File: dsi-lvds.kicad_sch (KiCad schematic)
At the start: 55 parts, among them J14 F52R-1A7H1-11020, J15 Conn_FFC_Amphenol_62684-40210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, U16 SN65DSI84

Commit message: [#54231] Add DSI/LVDS converter
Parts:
- removed C62, C63, C66, C67, C68, C69: C_100n_0402, antmicro-footprints:C_0402_1005Metric, symbol antmicroCapacitors0402:C_100n_0402
- removed C65: C_4u7_0402, antmicro-footprints:C_0402_1005Metric, symbol antmicroCapacitors0402:C_4u7_0402
- removed D22, D23, D24, D25, D26, D27, D28: PUSB3F96X_PASS, antmicro-footprints:Nexperia_DFN-10_2.5x1mm_P0.5mm, symbol antmicroTVSDiodes:PUSB3F96X_PASS
- removed J14: F52R-1A7H1-11020, antmicro-footprints:F52R-1A7H1-11020, symbol antmicroFCCConnectors:F52R-1A7H1-11020
- removed J15: Conn_FFC_Amphenol_62684-402100AHLF, antmicro-footprints:Conn_FFC_Amphenol_1x40_62684-402100AHLF, symbol antmicroFCCConnectors:FFC_Amphenol_1x40_62684-402100AHLF
- removed L10, L11, L12, L13, L14, L15, L16, L17, L18, L19, L20, L21, L22, L8, L9: NFP0QHB242HS2D, antmicro-footprints:Choke_025020_0605Metric, symbol antmicroCommonModeChokes:Choke_NFP0QHB242HS2D
- removed R106, R107, R109, R118, R120: R_10k_0402, antmicro-footprints:R_0402_1005Metric, symbol antmicroResistors0402:R_10k_0402
- removed R108, R117, R119, R121: R_0R_0402, antmicro-footprints:R_0402_1005Metric, symbol antmicroResistors0402:R_0R_0402
- removed R112, R113, R114, R115: R_2k2_0402, antmicro-footprints:R_0402_1005Metric, symbol antmicroResistors0402:R_2k2_0402
- removed TP12, TP13: TP_1.5mm_SMD, antmicro-footprints:TP_SMD_1.5mm, symbol antmicroTestPoints:TP_1.5mm_SMD
- removed TP14, TP15, TP16, TP17, TP18, TP19, TP20, TP21: TP_0.75mm_SMD, antmicro-footprints:TP_SMD_0.75mm, symbol antmicroTestPoints:TP_0.75mm_SMD
- added C? (x2): C_1u_0402, antmicro-footprints:C_0402_1005Metric, symbol antmicroCapacitors0402:C_1u_0402
- added C? (x5): C_100n_0402, antmicro-footprints:C_0402_1005Metric, symbol antmicroCapacitors0402:C_100n_0402
- added C? (x3): C_10n_0402, antmicro-footprints:C_0402_1005Metric, symbol antmicroCapacitors0402:C_10n_0402
- added C?: C_10u_0402, antmicro-footprints:C_0402_1005Metric, symbol antmicroCapacitors0402:C_10u_0402
- added FB?: 220Z/2A, antmicro-footprints:FB_0603_1608Metric, symbol antmicroFerriteBeadsandChips:FB_220Z_2.2A_TDK-MPZ_0603
- added R? (x3): R_10k_0402, antmicro-footprints:R_0402_1005Metric, symbol antmicroResistors0402:R_10k_0402
- added R? (x2): R_4k7_0402, antmicro-footprints:R_0402_1005Metric, symbol antmicroResistors0402:R_4k7_0402
- added U?: TXB0104_UQFN, antmicro-footprints:UQFN-12_2x1.7mm_P0.4mm_Texas_RUT, symbol antmicroLogicTranslatorsLevelShifters:TXB0104_UQFN
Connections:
- net SoMtoDisplay_Ferr_D3_N is gone; now on net DSI.D3_N: U16.30 (DA3N)
- net +3V3: now also C?.2, U?.11 (VCCB)
- net DSI.CLK_N: now also U16.25 (DACN)
- net DSI.CLK_P: now also U16.24 (DACP)
- net DSI.D0_N: now also U16.20 (DA0N)
- net DSI.D0_P: now also U16.19 (DA0P)
- net DSI.D1_N: now also U16.22 (DA1N)
- net DSI.D1_P: now also U16.21 (DA1P)
- net DSI.D2_N: now also U16.28 (DA2N)
- net DSI.D2_P: now also U16.27 (DA2P)
- net DSI.D3_P: now also U16.29 (DA3P)
- net GND: now also U16.23 (GND), U16.26 (GND), U16.52 (GND), U16.65 (PAD), C?.1, C?.1, C?.1, C?.1, C?.1, C?.1, C?.1, C?.1, C?.1, C?.1, C?.1, R?.1, R?.2, U?.6 (GND)
- net LVDS.CLK_N: now reaches U16.39 (A_CLKN)
- net at U16.14 (VCC), U16.18 (VCC), U16.3 (VCC)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: now also C?.2, C?.2, C?.2, C?.2, C?.2, C?.2, C?.2, C?.2, FB?.2
- net at U16.17 (REFCLK): now also R?.1
- net DSI/LVDS.EN: now reaches U16.2 (EN)
- net DSI/LVDS.EN: now also U?.4 (A3), U?.8 (B3)
- net at U16.31 (VCORE): now also C?.2
- net DSI/LVDS.IRQ: now reaches U16.33 (IRQ)
- net DSI/LVDS.IRQ: now also U?.5 (A4), U?.7 (B4)
- net LVDS.D3_P: now reaches U16.36 (A_Y3P)
- net LVDS.D3_N: now reaches U16.37 (A_Y3N)
- net LVDS.CLK_P: now reaches U16.38 (A_CLKP)
- net LVDS.D2_P: now reaches U16.41 (A_Y2P)
- net LVDS.D2_N: now reaches U16.42 (A_Y2N)
- net LVDS.D1_P: now reaches U16.44 (A_Y1P)
- net LVDS.D1_N: now reaches U16.45 (A_Y1N)
- net LVDS.D0_P: now reaches U16.46 (A_Y0P)
- net LVDS.D0_N: now reaches U16.47 (A_Y0N)
- net at U16.64 (ADDR): now also R?.1, R?.2
- net I_{2}C_DSI/LVDS.SCL renamed DSI/LVDS.SCL
- net DSI/LVDS.SCL: now also R?.1, U?.3 (A2), U?.9 (B2)
- net I_{2}C_DSI/LVDS.SDA renamed DSI/LVDS.SDA
- net DSI/LVDS.SDA: now also R?.1, U?.10 (B1), U?.2 (A1)
- new net +1V8: C?.2, FB?.1, R?.2, R?.2, R?.2, U?.1 (VCCA), U?.12 (OE)
- no-connect marks 3 -> 10
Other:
- note added: "Note: I_{2}C address selection: ADDR | write address 1 | 0x5A 0 | 0x58"
- note added: "Note: SN65DSI83*-Q1 should be here drop-in compatible"
- note removed: "Global reset (active low)"
- note removed: "LVDS connector"
- note removed: "Max 45mA"
- note removed: "Set display orientation as NORMAL datasheet pg.10"
- note removed: "TODO"
- note removed: "VDD"
- note removed: "Vcom"
- note removed: "assembly option for DSI connector (eg. pass-through to LVDS converter)"
- note removed: "select 8bit input"
- note removed: "select normal operation"

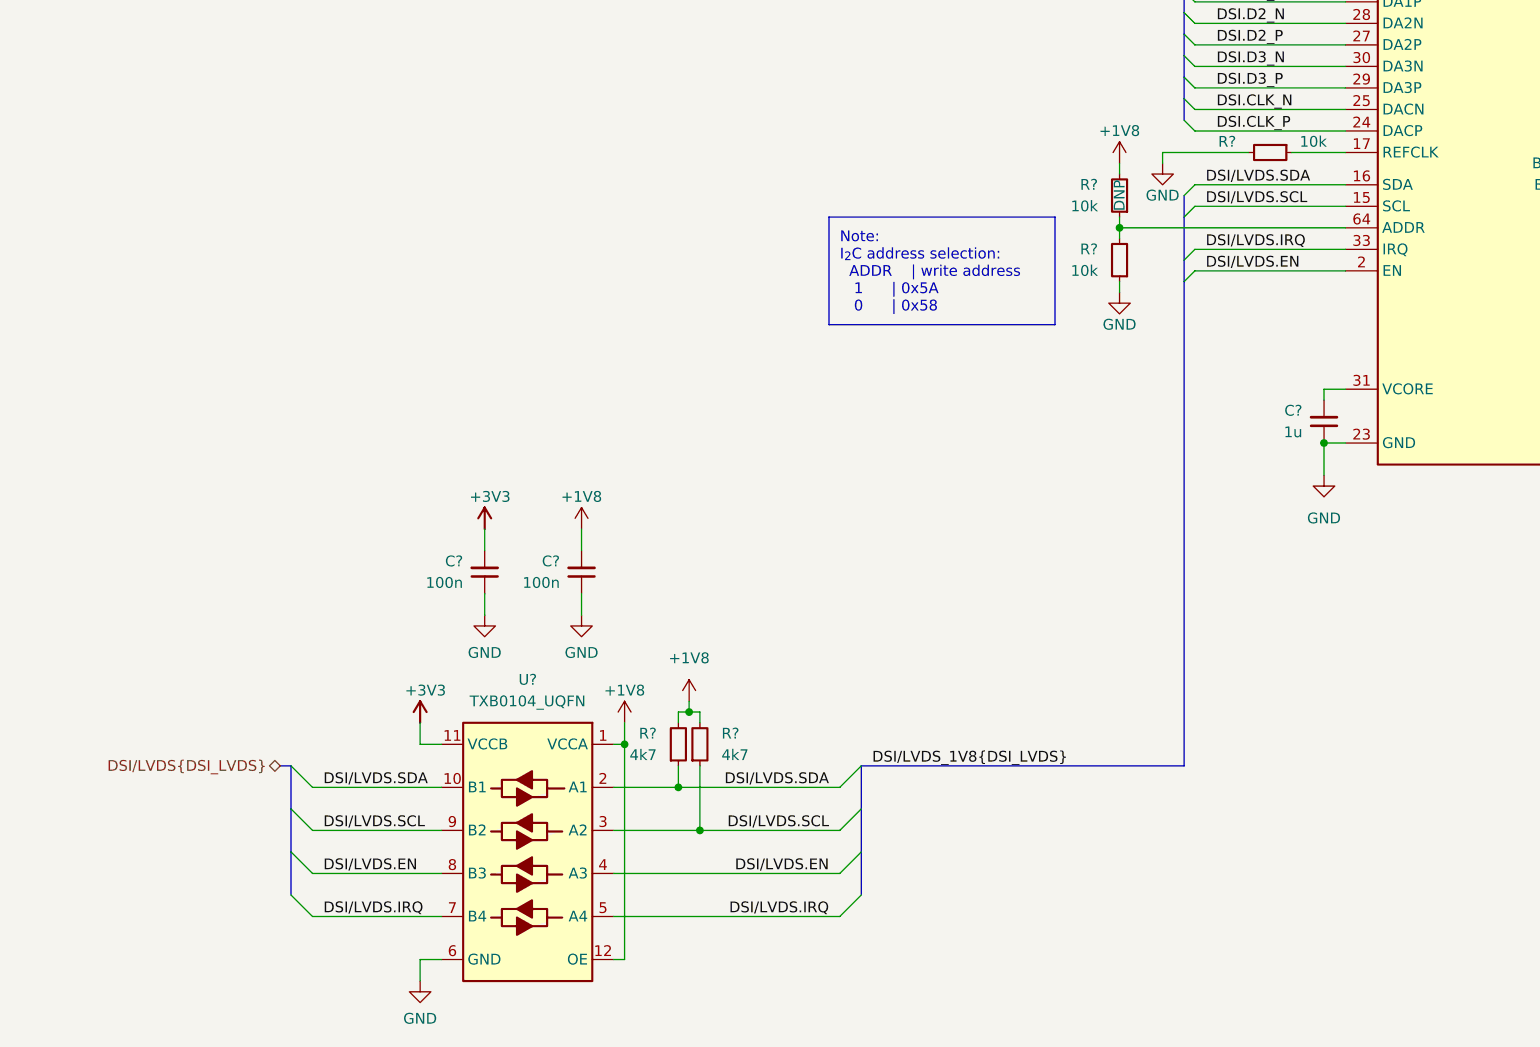
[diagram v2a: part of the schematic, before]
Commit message: [#54231] Rename bus DSI/LVDS to DisplayCtrl
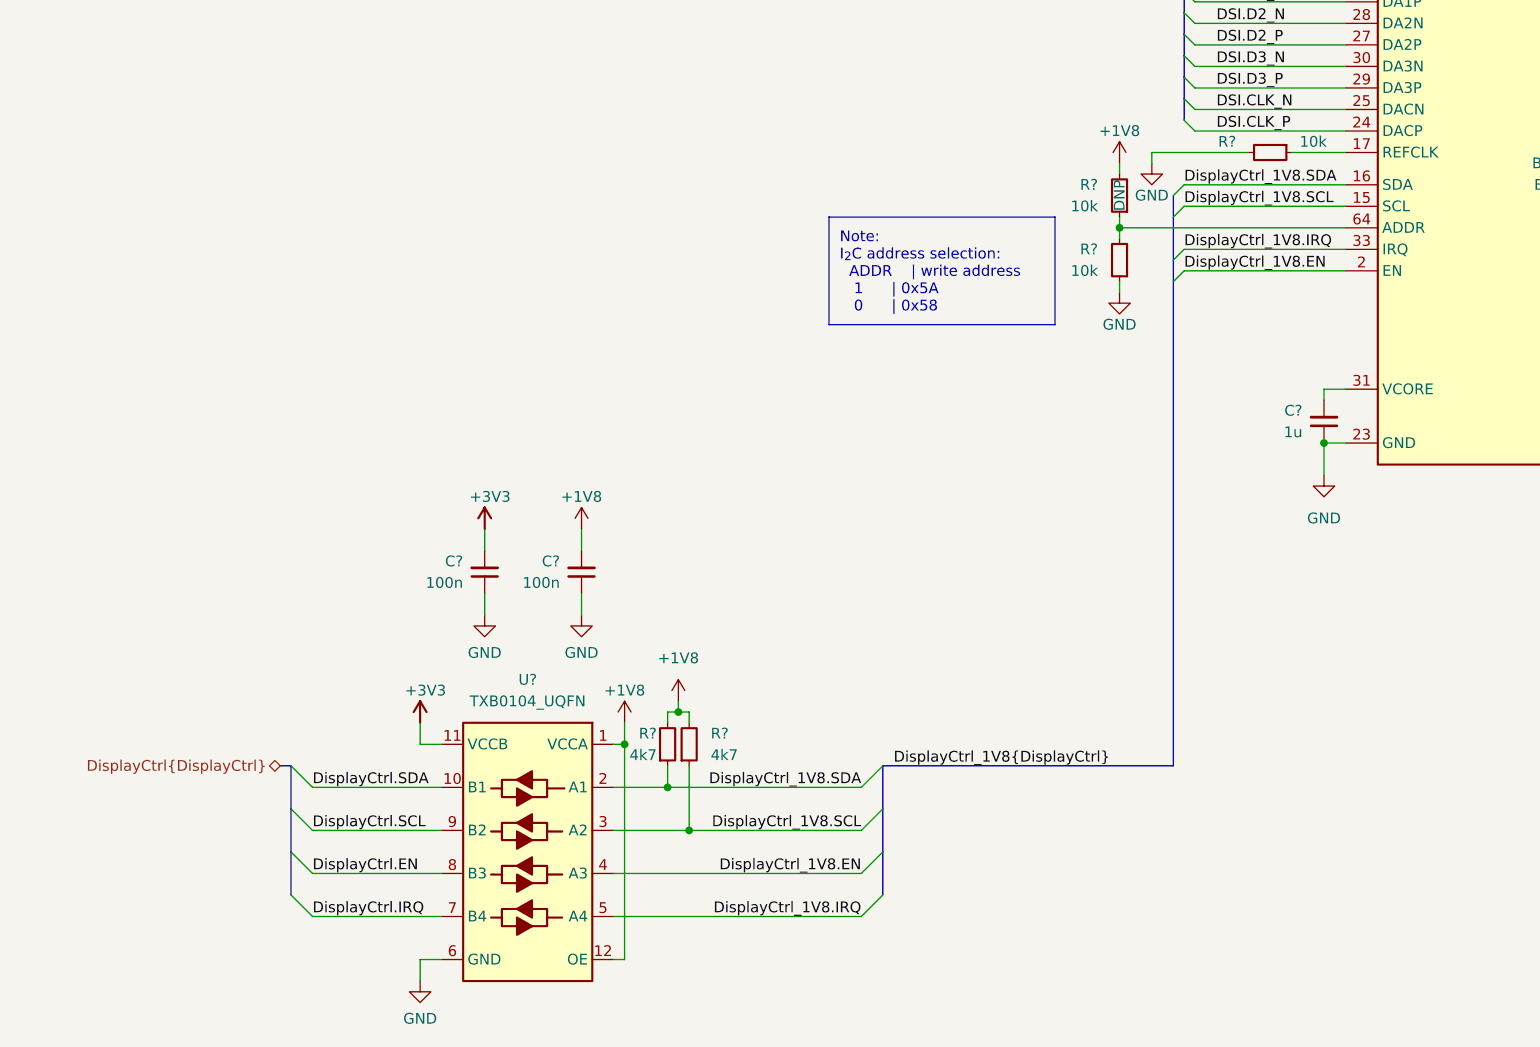
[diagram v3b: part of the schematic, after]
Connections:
- net DSI/LVDS.EN renamed DisplayCtrl_1V8.EN
- net DisplayCtrl_1V8.EN: no longer U?.8 (B3)
- net DSI/LVDS.IRQ renamed DisplayCtrl_1V8.IRQ
- net DisplayCtrl_1V8.IRQ: no longer U?.7 (B4)
- net DSI/LVDS.SCL renamed DisplayCtrl_1V8.SCL
- net DisplayCtrl_1V8.SCL: no longer U?.9 (B2)
- net DSI/LVDS.SDA renamed DisplayCtrl_1V8.SDA
- net DisplayCtrl_1V8.SDA: no longer U?.10 (B1)
- new net DisplayCtrl.EN: U?.8 (B3)
- new net DisplayCtrl.IRQ: U?.7 (B4)
- new net DisplayCtrl.SCL: U?.9 (B2)
- new net DisplayCtrl.SDA: U?.10 (B1)
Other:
- moved on the sheet: R?

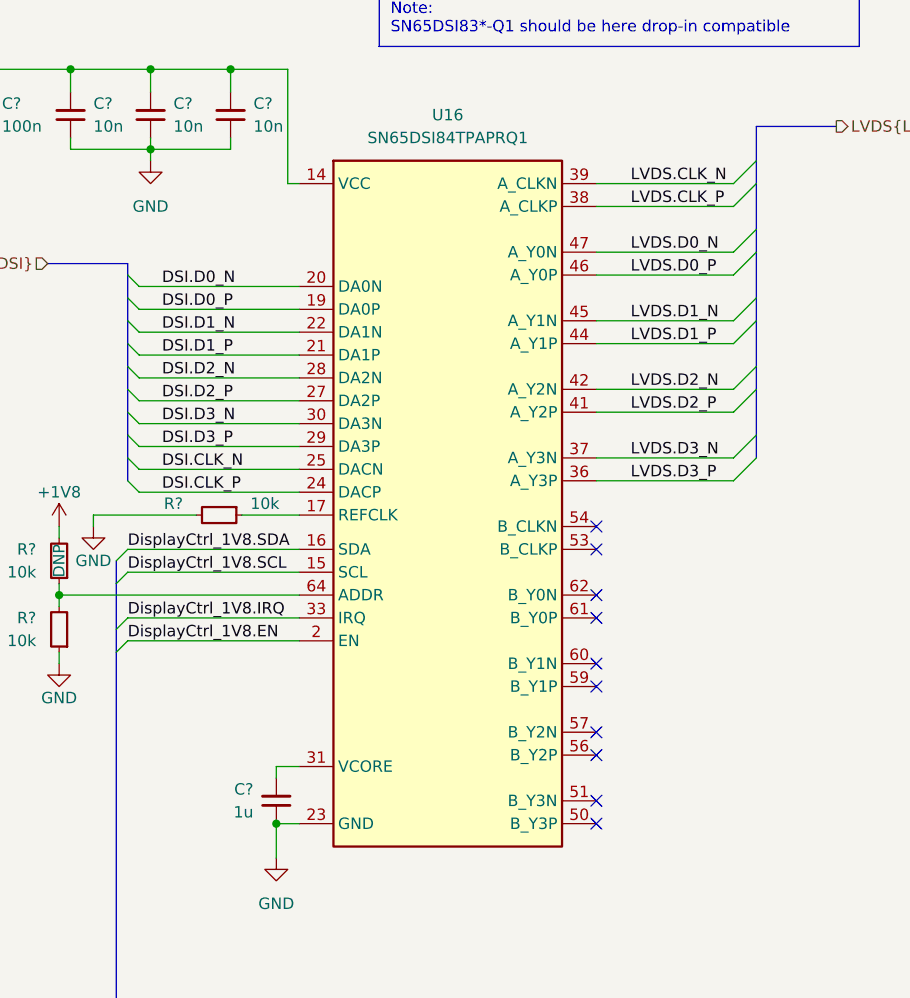
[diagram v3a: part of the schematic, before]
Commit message: [#54617] Update SN65DSI84 symbol
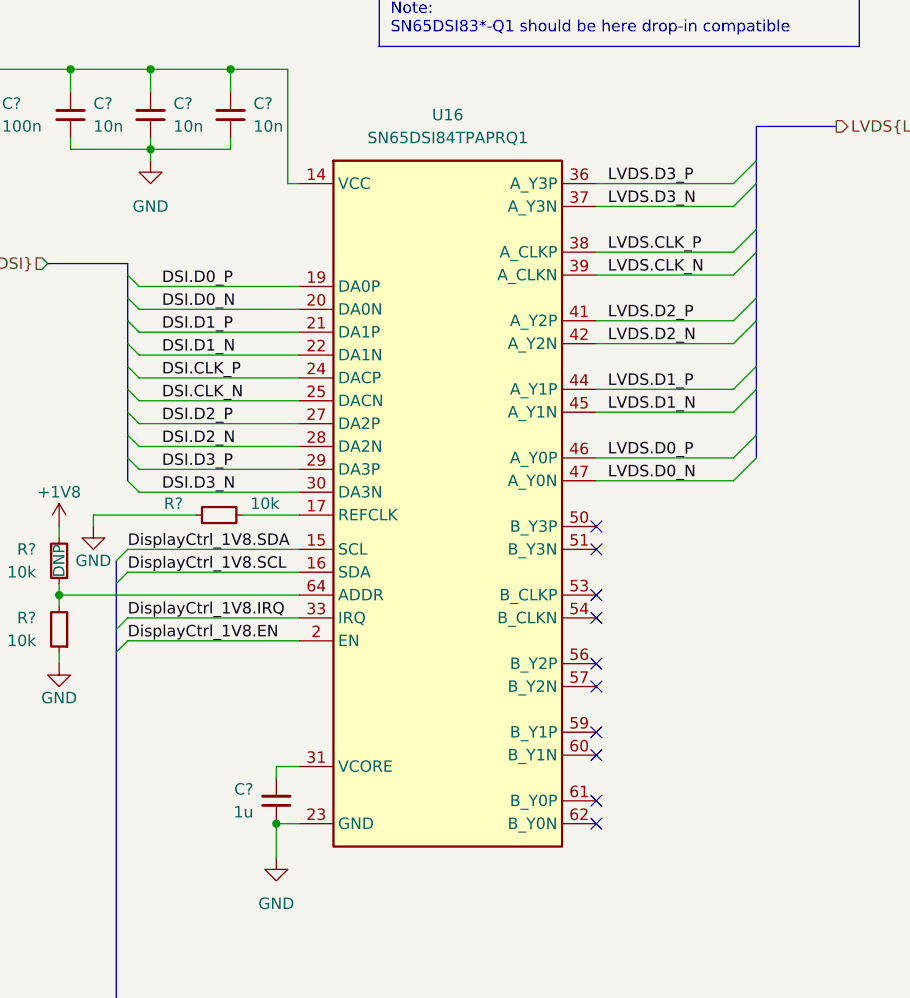
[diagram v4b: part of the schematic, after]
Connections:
- net DisplayCtrl_1V8.SCL: now also U16.16 (SDA); no longer U16.15 (SCL)
- net DisplayCtrl_1V8.SDA: now also U16.15 (SCL); no longer U16.16 (SDA)
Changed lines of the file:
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@@
     (effects (font (size 1.27 1.27)) (justify left bottom))
   )
-  (label "DSI.D3_P" (at 231.14 120.65 0)
+  (label "DSI.D3_P" (at 231.14 123.19 0)
     (effects (font (size 1.27 1.27)) (justify left bottom))
   )
-  (label "LVDS.D0_N" (at 283.21 99.06 0)
+  (label "LVDS.D0_N" (at 280.67 124.46 0)
     (effects (font (size 1.27 1.27)) (justify left bottom))
   )
-  (label "LVDS.D2_N" (at 283.21 114.3 0)
+  (label "LVDS.D2_N" (at 280.67 109.22 0)
     (effects (font (size 1.27 1.27)) (justify left bottom))
   )
@@
     (effects (font (size 1.27 1.27)) (justify left bottom))
   )
-  (label "LVDS.D1_N" (at 283.21 106.68 0)
+  (label "LVDS.D1_N" (at 280.67 116.84 0)
     (effects (font (size 1.27 1.27)) (justify left bottom))
   )
@@
     (effects (font (size 1.27 1.27)) (justify right bottom))
   )
-  (label "LVDS.CLK_P" (at 283.21 93.98 0)
+  (label "LVDS.CLK_P" (at 280.67 99.06 0)
     (effects (font (size 1.27 1.27)) (justify left bottom))
   )
-  (label "DSI.D1_P" (at 231.14 110.49 0)
+  (label "DSI.D1_P" (at 231.14 107.95 0)
     (effects (font (size 1.27 1.27)) (justify left bottom))
   )
-  (label "LVDS.D1_P" (at 283.21 109.22 0)
+  (label "LVDS.D1_P" (at 280.67 114.3 0)
     (effects (font (size 1.27 1.27)) (justify left bottom))
   )
-  (label "LVDS.D3_N" (at 283.21 121.92 0)
+  (label "LVDS.D3_N" (at 280.67 93.98 0)
     (effects (font (size 1.27 1.27)) (justify left bottom))
   )
-  (label "LVDS.CLK_N" (at 283.21 91.44 0)
+  (label "LVDS.CLK_N" (at 280.67 101.6 0)
     (effects (font (size 1.27 1.27)) (justify left bottom))
   )
-  (label "DSI.CLK_P" (at 231.14 125.73 0)
+  (label "DSI.CLK_P" (at 231.14 113.03 0)
     (effects (font (size 1.27 1.27)) (justify left bottom))
   )
@@
     (effects (font (size 1.27 1.27)) (justify left bottom))
   )
-  (label "LVDS.D0_P" (at 283.21 101.6 0)
+  (label "LVDS.D0_P" (at 280.67 121.92 0)
     (effects (font (size 1.27 1.27)) (justify left bottom))
   )
-  (label "LVDS.D2_P" (at 283.21 116.84 0)
+  (label "LVDS.D2_P" (at 280.67 106.68 0)
     (effects (font (size 1.27 1.27)) (justify left bottom))
   )
@@
     (effects (font (size 1.27 1.27)) (justify right bottom))
   )
-  (label "DSI.D2_P" (at 231.14 115.57 0)
+  (label "DSI.D2_P" (at 231.14 118.11 0)
     (effects (font (size 1.27 1.27)) (justify left bottom))
   )
@@
     (effects (font (size 1.27 1.27)) (justify left bottom))
   )
-  (label "DSI.CLK_N" (at 231.14 123.19 0)
+  (label "DSI.CLK_N" (at 231.14 115.57 0)
     (effects (font (size 1.27 1.27)) (justify left bottom))
   )
-  (label "LVDS.D3_P" (at 283.21 124.46 0)
+  (label "LVDS.D3_P" (at 280.67 91.44 0)
     (effects (font (size 1.27 1.27)) (justify left bottom))
   )
-  (label "DSI.D0_N" (at 231.14 102.87 0)
+  (label "DSI.D0_N" (at 231.14 105.41 0)
     (effects (font (size 1.27 1.27)) (justify left bottom))
   )
-  (label "DSI.D0_P" (at 231.14 105.41 0)
+  (label "DSI.D0_P" (at 231.14 102.87 0)
     (effects (font (size 1.27 1.27)) (justify left bottom))
   )
-  (label "DSI.D3_N" (at 231.14 118.11 0)
+  (label "DSI.D3_N" (at 231.14 125.73 0)
     (effects (font (size 1.27 1.27)) (justify left bottom))
   )
@@
     (effects (font (size 1.27 1.27)) (justify left bottom))
   )
-  (label "DSI.D1_N" (at 231.14 107.95 0)
+  (label "DSI.D1_N" (at 231.14 110.49 0)
     (effects (font (size 1.27 1.27)) (justify left bottom))
   )
-  (label "DSI.D2_N" (at 231.14 113.03 0)
+  (label "DSI.D2_N" (at 231.14 120.65 0)
     (effects (font (size 1.27 1.27)) (justify left bottom))
   )
